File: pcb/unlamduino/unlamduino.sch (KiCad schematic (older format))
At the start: 41 parts, among them IC2 ATMEGA328-P, P3 CONN_01X08, U1 LM2576, U2 AP111733, Y2 16MHz

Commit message: Corrección separación de patas del inductor de la fuente.
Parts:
- L3: footprint Choke_Toroid_ThroughHole:Choke_Toroid_horizontal_Diameter4-5mm_Amidon-T16 -> Choke_Toroid_ThroughHole:Choke_Toroid_5x10mm_Vertical
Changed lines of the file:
@@
 F 0 "L3" V 6000 1950 50  0000 L CNN
 F 1 "330uHy" V 5900 1850 50  0000 L CNN
-F 2 "Choke_Toroid_ThroughHole:Choke_Toroid_horizontal_Diameter4-5mm_Amidon-T16" H 6050 2000 50  0001 C CNN
+F 2 "Choke_Toroid_ThroughHole:Choke_Toroid_5x10mm_Vertical" H 6050 2000 50  0001 C CNN
 F 3 "" H 6050 2000 50  0000 C CNN
 	1    6050 2000

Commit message: Cambio separacion de patas de C7
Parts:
- C7: footprint Capacitors_ThroughHole:C_Disc_D3_P2.5 -> Capacitors_ThroughHole:C_Disc_D6_P5
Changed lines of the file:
@@
 F 0 "C7" H 2275 4100 50  0000 L CNN
 F 1 "100nF" H 2275 3900 50  0000 L CNN
-F 2 "Capacitors_ThroughHole:C_Disc_D3_P2.5" H 2288 3850 50  0001 C CNN
+F 2 "Capacitors_ThroughHole:C_Disc_D6_P5" H 2288 3850 50  0001 C CNN
 F 3 "" H 2250 4000 50  0000 C CNN
 	1    2250 4000

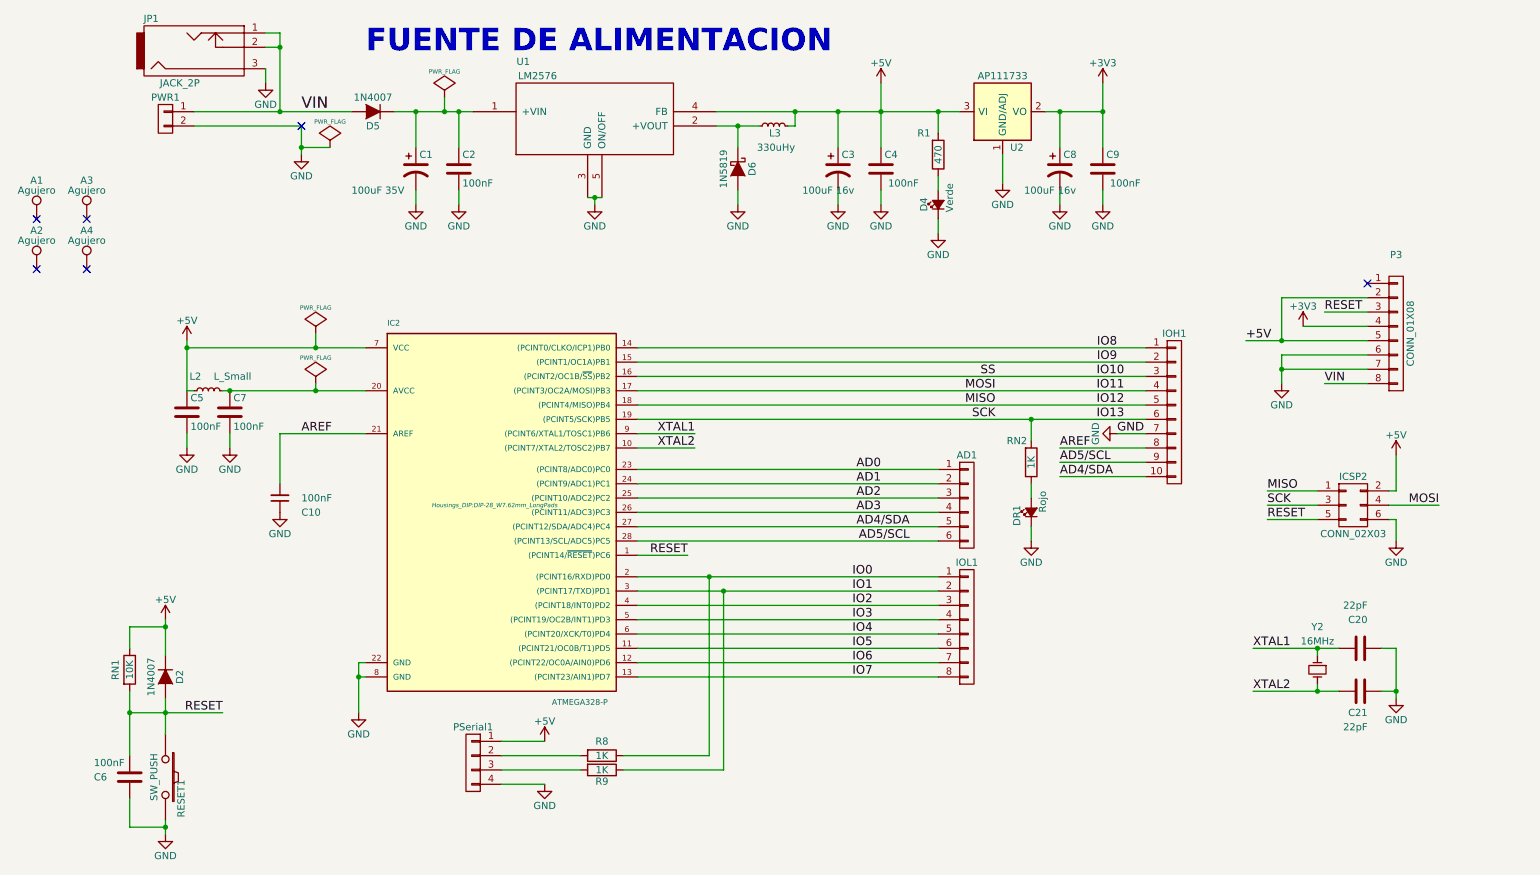
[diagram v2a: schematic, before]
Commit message: unlamduino.sch: Agregu agujeros faltantes, quito etiqueta 5V, leyenda ISP, detalles de uniones.
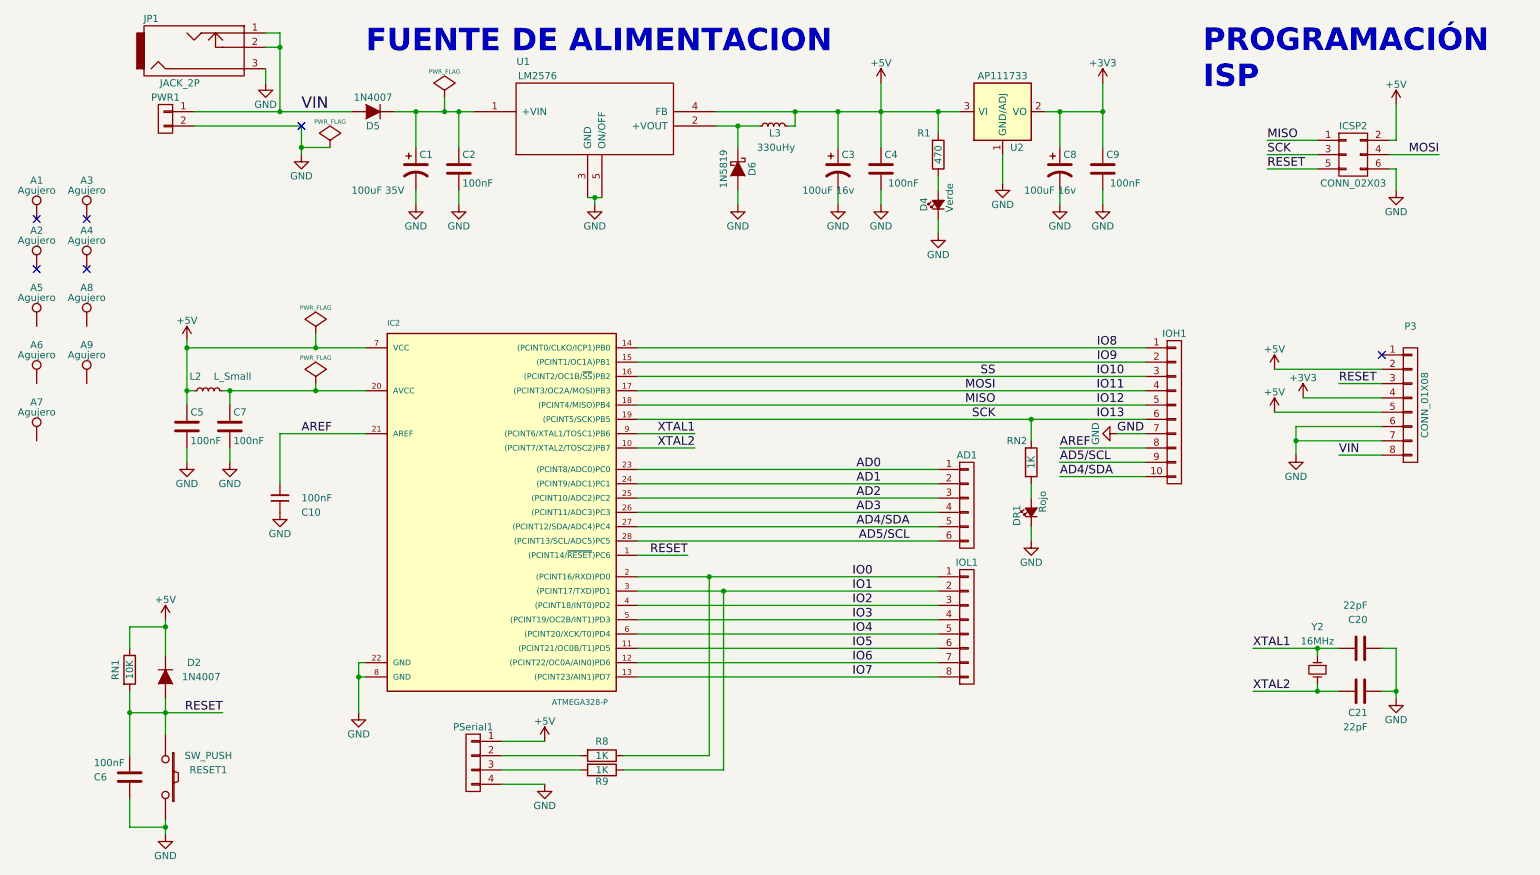
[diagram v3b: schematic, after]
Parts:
- added A5, A6, A7, A8, A9: Agujero, Mounting_Holes:MountingHole_3.2mm_M3, symbol TEST_1P
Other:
- note added: "PROGRAMACIÓN\nISP"
- moved on the sheet: C5, C7, ICSP2, P3

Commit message: Cambio el footprint asociado del inductor de fuente del unlamduino.
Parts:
- L3: footprint Choke_Toroid_ThroughHole:Choke_Toroid_5x10mm_Vertical -> huellas:INDUCTOR_V
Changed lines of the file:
@@
 F 0 "L3" V 6000 1950 50  0000 L CNN
 F 1 "330uHy" V 5900 1850 50  0000 L CNN
-F 2 "Choke_Toroid_ThroughHole:Choke_Toroid_5x10mm_Vertical" H 6050 2000 50  0001 C CNN
+F 2 "huellas:INDUCTOR_V" H 6050 2000 50  0001 C CNN
 F 3 "" H 6050 2000 50  0000 C CNN
 	1    6050 2000

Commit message: Unlamduino .sch: cambio footprint del inductor del A/D por uno más chico 10mm  a 7mm.
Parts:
- L2: footprint Resistors_ThroughHole:Resistor_Horizontal_RM10mm -> huellas:Resistor_Horizontal_RM7mm
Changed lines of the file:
@@
 F 0 "L2" V 2200 3900 50  0000 L CNN
 F 1 "L_Small" V 2200 3550 50  0000 L CNN
-F 2 "Resistors_ThroughHole:Resistor_Horizontal_RM10mm" H 2100 3850 50  0001 C CNN
+F 2 "huellas:Resistor_Horizontal_RM7mm" H 2100 3850 50  0001 C CNN
 F 3 "" H 2100 3850 50  0000 C CNN
 	1    2100 3850

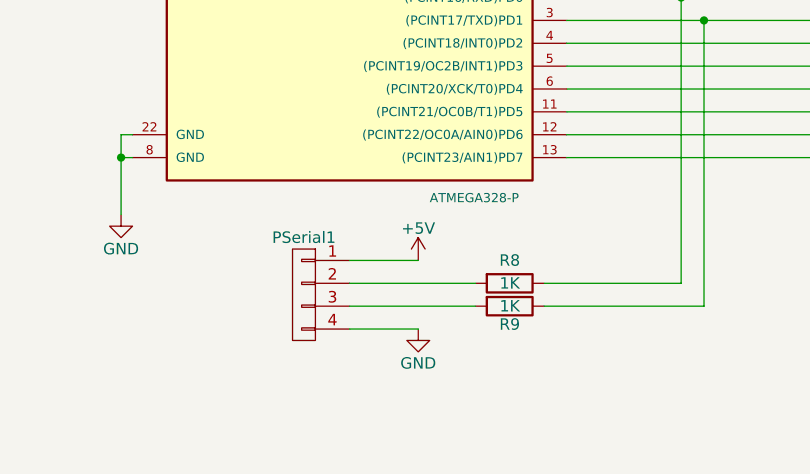
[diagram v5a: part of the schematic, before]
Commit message: Agrego señales rx y tx en el conector serie para identificar en el PCB.
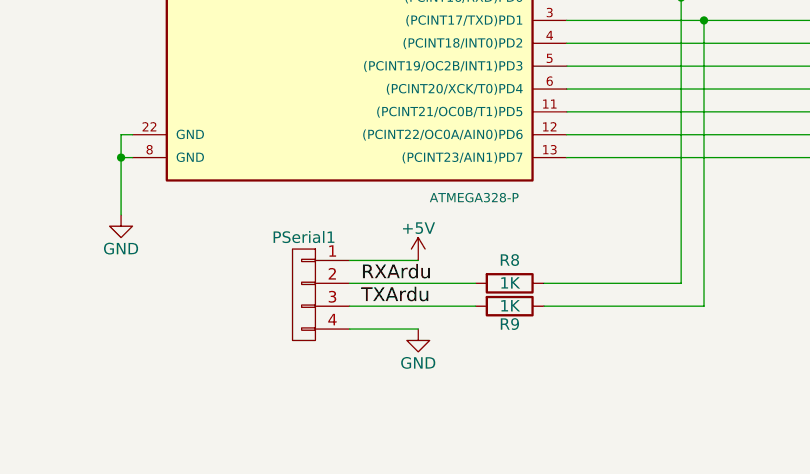
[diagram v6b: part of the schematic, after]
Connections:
- net RXArdu: now reaches PSerial1.2 (P2), R8.2
- net TXArdu: now reaches PSerial1.3 (P3), R9.2
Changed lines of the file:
@@
 	1    0    0    -1
 $EndComp
+Text Label 4200 6400 0    60   ~ 0
+RXArdu
+Text Label 4200 6500 0    60   ~ 0
+TXArdu
 $EndSCHEMATC

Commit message: Completo vista 3D
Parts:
- L2: footprint huellas:Resistor_Horizontal_RM7mm -> huellas:Resistor_Horizontal_RM7mm3d
- R1, R8, R9, RN1, RN2: footprint Resistors_ThroughHole:Resistor_Horizontal_RM7mm -> huellas:Resistor_Horizontal_RM7mm3d
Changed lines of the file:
@@
 F 0 "R8" V 4750 6400 50  0000 C CNN
 F 1 "1K" V 4850 6400 50  0000 C CNN
-F 2 "Resistors_ThroughHole:Resistor_Horizontal_RM7mm" V 4780 6400 50  0001 C CNN
+F 2 "huellas:Resistor_Horizontal_RM7mm3d" V 4780 6400 50  0001 C CNN
 F 3 "" H 4850 6400 50  0000 C CNN
 	1    4850 6400
@@
 F 0 "R9" V 4930 6500 50  0000 C CNN
 F 1 "1K" V 4850 6500 50  0000 C CNN
-F 2 "Resistors_ThroughHole:Resistor_Horizontal_RM7mm" V 4780 6500 50  0001 C CNN
+F 2 "huellas:Resistor_Horizontal_RM7mm3d" V 4780 6500 50  0001 C CNN
 F 3 "" H 4850 6500 50  0000 C CNN
 	1    4850 6500
@@
 F 0 "L2" V 2200 3900 50  0000 L CNN
 F 1 "L_Small" V 2200 3550 50  0000 L CNN
-F 2 "huellas:Resistor_Horizontal_RM7mm" H 2100 3850 50  0001 C CNN
+F 2 "huellas:Resistor_Horizontal_RM7mm3d" H 2100 3850 50  0001 C CNN
 F 3 "" H 2100 3850 50  0000 C CNN
 	1    2100 3850
@@
 F 0 "RN1" V 1450 5800 50  0000 C CNN
 F 1 "10K" V 1550 5800 50  0000 C CNN
-F 2 "Resistors_ThroughHole:Resistor_Horizontal_RM7mm" V 1480 5800 50  0001 C CNN
+F 2 "huellas:Resistor_Horizontal_RM7mm3d" V 1480 5800 50  0001 C CNN
 F 3 "" H 1550 5800 50  0000 C CNN
 	1    1550 5800
@@
 F 0 "R1" H 7100 2050 50  0000 C CNN
 F 1 "470" V 7200 2200 50  0000 C CNN
-F 2 "Resistors_ThroughHole:Resistor_Horizontal_RM7mm" V 7130 2200 50  0001 C CNN
+F 2 "huellas:Resistor_Horizontal_RM7mm3d" V 7130 2200 50  0001 C CNN
 F 3 "" H 7200 2200 50  0000 C CNN
 	1    7200 2200
@@
 F 0 "RN2" H 7750 4200 50  0000 C CNN
 F 1 "1K" V 7850 4350 50  0000 C CNN
-F 2 "Resistors_ThroughHole:Resistor_Horizontal_RM7mm" V 7780 4350 50  0001 C CNN
+F 2 "huellas:Resistor_Horizontal_RM7mm3d" V 7780 4350 50  0001 C CNN
 F 3 "" H 7850 4350 50  0000 C CNN
 	1    7850 4350

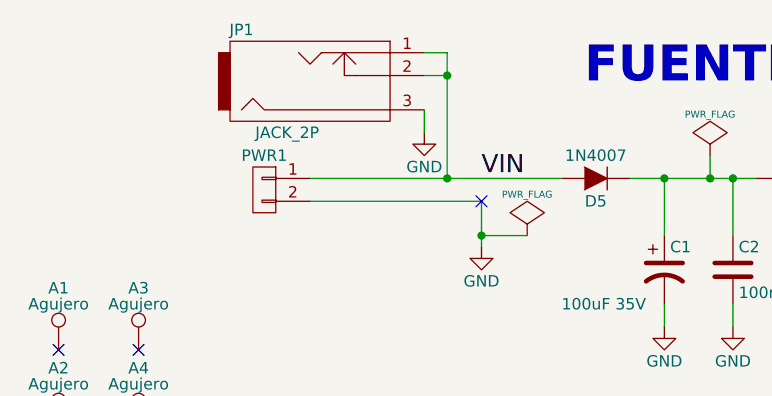
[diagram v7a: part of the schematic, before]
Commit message: Cambio de conector de alimentacion que estaba erroneo.
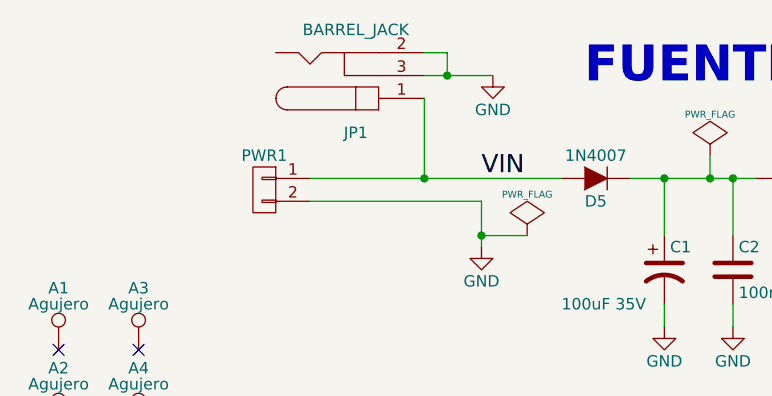
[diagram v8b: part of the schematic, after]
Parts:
- removed JP1: JACK_2P, Connect:BARREL_JACK, symbol JACK_2P
- added JP1: BARREL_JACK, symbol BARREL_JACK
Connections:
- net GND: now also JP1.2, JP1.3
- net VIN: now also JP1.1
- no-connect marks 6 -> 5
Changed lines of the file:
@@
 EESchema Schematic File Version 2
-LIBS:power
+LIBS:conn
 LIBS:unlamduino-cache
 EELAYER 25 0
@@
 	-1   0    0    -1
 $EndComp
-$Comp
-L JACK_2P JP1
-U 1 1 57F5A399
-P 2050 1450
-F 0 "JP1" H 1700 1250 50  0000 C CNN
-F 1 "JACK_2P" H 1900 1700 50  0000 C CNN
-F 2 "Connect:BARREL_JACK" H 2050 1450 50  0001 C CNN
-F 3 "" H 2050 1450 50  0000 C CNN
-	1    2050 1450
-	1    0    0    1
-$EndComp
 Wire Wire Line
 	2500 1350 2600 1350
-Wire Wire Line
-	2600 1350 2600 1900
-Connection ~ 2600 1900
+Connection ~ 2500 1900
 $Comp
 L GND-RESCUE-UNLAMDIUNO #PWR029
 U 1 1 57F5A7AF
-P 2500 1700
-F 0 "#PWR029" H 2500 1450 50  0001 C CNN
-F 1 "GND" H 2500 1550 50  0000 C CNN
-F 2 "" H 2500 1700 50  0000 C CNN
-F 3 "" H 2500 1700 50  0000 C CNN
-	1    2500 1700
-	1    0    0    -1
-$EndComp
-Wire Wire Line
-	2500 1600 2500 1700
-Wire Wire Line
-	2500 1450 2600 1450
+P 2800 1450
+F 0 "#PWR029" H 2800 1200 50  0001 C CNN
+F 1 "GND" H 2800 1300 50  0000 C CNN
+F 2 "" H 2800 1450 50  0000 C CNN
+F 3 "" H 2800 1450 50  0000 C CNN
+	1    2800 1450
+	1    0    0    -1
+$EndComp
+Wire Wire Line
+	2500 1450 2800 1450
 Connection ~ 2600 1450
 $Comp
@@
 $EndComp
 NoConn ~ 900  2650
-NoConn ~ 2750 2000
 $Comp
 L TEST_1P A3
@@
 Text Label 4200 6500 0    60   ~ 0
 TXArdu
+$Comp
+L BARREL_JACK JP1
+U 1 1 5839A0A2
+P 2200 1450
+F 0 "JP1" H 2200 1700 50  0000 C CNN
+F 1 "BARREL_JACK" H 2200 1250 50  0000 C CNN
+F 2 "" H 2200 1450 50  0000 C CNN
+F 3 "" H 2200 1450 50  0000 C CNN
+	1    2200 1450
+	1    0    0    1
+$EndComp
+Wire Wire Line
+	2600 1350 2600 1450
+Wire Wire Line
+	2500 1900 2500 1550
 $EndSCHEMATC
